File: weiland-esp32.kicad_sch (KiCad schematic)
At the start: 19 parts, among them J1 Conn_01x04_Pin, J3 Conn_01x04_Pin, J5 Conn_02x03_Odd_Even, U1 ESP32-WROOM-32E(8MB), U2 AMS1117-3.3_C347222, U3 GR6205-SOP-8, U4 MAX98357AEWL_T

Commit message: routing draft completed
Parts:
- removed J3: Conn_01x04_Pin, Connector_Wire:SolderWire-0.75sqmm_1x04_P4.8mm_D1.25mm_OD2.3mm, symbol Connector:Conn_01x04_Pin
- added J2: Conn_01x05_Pin, customlibrary:SolderWire-0.75sqmm_1x05_P4.8mm_D1.25mm_OD2.3mm, symbol Connector:Conn_01x05_Pin
- J5: footprint (none) -> Connector_PinSocket_1.27mm:PinSocket_2x03_P1.27mm_Vertical_SMD
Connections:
- net +5V_EXT is gone; now on net +5V: C3.2, J5.2 (Pin_2)
- net +5V: now also U4.A1 (SD_MODE), J2.5 (Pin_5)
- net GND: now also J2.4 (Pin_4)
- net OUTB: now also J2.3 (Pin_3)
- net OUTN: now also J2.2 (Pin_2)
- net OUTP: now also J2.1 (Pin_1)
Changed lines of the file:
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@@
 	(wire
 		(pts
-			(xy 55.88 60.96) (xy 44.45 60.96)
+			(xy 35.56 60.96) (xy 27.94 60.96)
 		)
 		(stroke
@@
 	(wire
 		(pts
-			(xy 44.45 55.88) (xy 52.07 55.88)
+			(xy 27.94 55.88) (xy 31.75 55.88)
 		)
 		(stroke
@@
 	(wire
 		(pts
-			(xy 44.45 58.42) (xy 52.07 58.42)
+			(xy 27.94 58.42) (xy 31.75 58.42)
 		)
 		(stroke
@@
 	(wire
 		(pts
+			(xy 218.44 173.99) (xy 219.71 173.99)
+		)
+		(stroke
+			(width 0)
+			(type default)
+		)
+	)
+	(wire
+		(pts
 			(xy 57.15 119.38) (xy 36.83 119.38)
 		)
@@
 	(wire
 		(pts
+			(xy 218.44 179.07) (xy 218.44 173.99)
+		)
+		(stroke
+			(width 0)
+			(type default)
+		)
+	)
+	(wire
+		(pts
 			(xy 255.27 163.83) (xy 295.91 163.83)
 		)
@@
 	(wire
 		(pts
+			(xy 27.94 66.04) (xy 30.48 66.04)
+		)
+		(stroke
+			(width 0)
+			(type default)
+		)
+	)
+	(wire
+		(pts
 			(xy 295.91 193.04) (xy 295.91 198.12)
 		)
@@
 	(wire
 		(pts
-			(xy 44.45 63.5) (xy 57.15 63.5)
+			(xy 27.94 63.5) (xy 36.83 63.5)
 		)
 		(stroke
@@
 	(wire
 		(pts
+			(xy 30.48 66.04) (xy 30.48 71.12)
+		)
+		(stroke
+			(width 0)
+			(type default)
+		)
+	)
+	(wire
+		(pts
 			(xy 124.46 30.48) (xy 124.46 39.37)
 		)
@@
 	)
 	(label "OUTB"
-		(at 54.61 60.96 0)
+		(at 34.29 60.96 0)
 		(fields_autoplaced yes)
 		(effects
@@
 	)
 	(label "OUTP"
-		(at 49.53 55.88 0)
+		(at 29.21 55.88 0)
 		(fields_autoplaced yes)
 		(effects
@@
 	)
 	(label "OUTN"
-		(at 50.8 58.42 0)
+		(at 30.48 58.42 0)
 		(fields_autoplaced yes)
 		(effects
@@
 	)
 	(symbol
-		(lib_id "Connector:Conn_01x04_Pin")
-		(at 39.37 58.42 0)
+		(lib_id "+5V")
+		(at 218.44 179.07 0)
+		(mirror y)
 		(unit 1)
 		(exclude_from_sim no)
@@
 		(on_board yes)
 		(dnp no)
-		(fields_autoplaced yes)
-		(property "Reference" "J3"
-			(at 40.005 50.8 0)
+		(property "Reference" "#PWR03"
+			(at 218.44 179.07 0)
 			(effects
 				(font
 					(size 1.27 1.27)
 				)
+				(hide yes)
 			)
 		)
-		(property "Value" "Conn_01x04_Pin"
-			(at 40.005 53.34 0)
+		(property "Value" "+5V"
+			(at 221.6912 182.0926 0)
 			(effects
 				(font
-					(size 1.27 1.27)
+					(face "Times New Roman")
+					(size 2.1717 2.1717)
 				)
+				(justify left top)
 			)
 		)
-		(property "Footprint" "Connector_Wire:SolderWire-0.75sqmm_1x04_P4.8mm_D1.25mm_OD2.3mm"
-			(at 39.37 58.42 0)
+		(property "Footprint" ""
+			(at 218.44 179.07 0)
 			(effects
 				(font
@@
 			)
 		)
-		(property "Datasheet" "~"
-			(at 39.37 58.42 0)
+		(property "Datasheet" ""
+			(at 218.44 179.07 0)
 			(effects
 				(font
@@
 			)
 		)
-		(property "Description" "Generic connector, single row, 01x04, script generated"
-			(at 39.37 58.42 0)
+		(property "Description" "Power symbol creates a global label with name '+5V'"
+			(at 218.44 179.07 0)
 			(effects
 				(font
@@
 			)
 		)
-		(pin "4"
-		)
-		(pin "2"
-		)
-		(pin "3"
-		)
 		(pin "1"
 		)
 		(instances
-			(project "esp32-online-design"
+			(project "weiland-esp32"
 				(path "/745a8d65-fa51-45f7-9665-7610e72f2a80"
-					(reference "J3")
-					(unit 1)
-				)
-			)
-			(project ""
-				(path "/a1dc64ca-b54e-4a93-b40f-f15a664195f8"
-					(reference "J6")
+					(reference "#PWR03")
 					(unit 1)
 				)
@@
 	)
 	(symbol
+		(lib_id "Connector:Conn_01x05_Pin")
+		(at 22.86 60.96 0)
+		(unit 1)
+		(exclude_from_sim no)
+		(in_bom yes)
+		(on_board yes)
+		(dnp no)
+		(fields_autoplaced yes)
+		(property "Reference" "J2"
+			(at 23.495 50.8 0)
+			(effects
+				(font
+					(size 1.27 1.27)
+				)
+			)
+		)
+		(property "Value" "Conn_01x05_Pin"
+			(at 23.495 53.34 0)
+			(effects
+				(font
+					(size 1.27 1.27)
+				)
+			)
+		)
+		(property "Footprint" "customlibrary:SolderWire-0.75sqmm_1x05_P4.8mm_D1.25mm_OD2.3mm"
+			(at 22.86 60.96 0)
+			(effects
+				(font
+					(size 1.27 1.27)
+				)
+				(hide yes)
+			)
+		)
+		(property "Datasheet" "~"
+			(at 22.86 60.96 0)
+			(effects
+				(font
+					(size 1.27 1.27)
+				)
+				(hide yes)
+			)
+		)
+		(property "Description" "Generic connector, single row, 01x05, script generated"
+			(at 22.86 60.96 0)
+			(effects
+				(font
+					(size 1.27 1.27)
+				)
+				(hide yes)
+			)
+		)
+		(pin "2"
+		)
+		(pin "1"
+		)
+		(pin "4"
+		)
+		(pin "5"
+		)
+		(pin "3"
+		)
+		(instances
+			(project ""
+				(path "/745a8d65-fa51-45f7-9665-7610e72f2a80"
+					(reference "J2")
+					(unit 1)
+				)
+			)
+		)
+	)
+	(symbol
 		(lib_id "CL21A226MAYNNNE")
 		(at 13.97 105.41 0)
@@
 			)
 		)
-		(property "Footprint" ""
+		(property "Footprint" "Connector_PinSocket_1.27mm:PinSocket_2x03_P1.27mm_Vertical_SMD"
 			(at 104.14 30.48 0)
 			(effects
@@
 	)
 	(symbol
-		(lib_id "+5V_EXT")
-		(at 129.54 25.4 0)
-		(mirror x)
+		(lib_id "+5V")
+		(at 30.48 71.12 0)
+		(mirror y)
 		(unit 1)
 		(exclude_from_sim no)
@@
 		(on_board yes)
 		(dnp no)
-		(property "Reference" "#PWR0104"
-			(at 129.54 25.4 0)
+		(property "Reference" "#PWR02"
+			(at 30.48 71.12 0)
 			(effects
 				(font
@@
 			)
 		)
-		(property "Value" "+5V_EXT"
-			(at 121.4628 21.6154 0)
+		(property "Value" "+5V"
+			(at 33.7312 74.1426 0)
 			(effects
 				(font
@@
 		)
 		(property "Footprint" ""
-			(at 129.54 25.4 0)
+			(at 30.48 71.12 0)
 			(effects
 				(font
@@
 		)
 		(property "Datasheet" ""
-			(at 129.54 25.4 0)
+			(at 30.48 71.12 0)
 			(effects
 				(font
@@
 			)
 		)
-		(property "Description" "Power symbol creates a global label with name '+5V_EXT'"
-			(at 129.54 25.4 0)
+		(property "Description" "Power symbol creates a global label with name '+5V'"
+			(at 30.48 71.12 0)
 			(effects
 				(font
@@
 		)
 		(instances
-			(project "esp32-online-design"
+			(project "weiland-esp32"
 				(path "/745a8d65-fa51-45f7-9665-7610e72f2a80"
-					(reference "#PWR0104")
+					(reference "#PWR02")
 					(unit 1)
 				)
@@
 	(symbol
 		(lib_id "GND")
-		(at 57.15 63.5 90)
+		(at 36.83 63.5 90)
 		(unit 1)
 		(exclude_from_sim no)
@@
 		(dnp no)
 		(property "Reference" "#PWR0101"
-			(at 57.15 63.5 0)
+			(at 36.83 63.5 0)
 			(effects
 				(font
@@
 		)
 		(property "Value" "GND"
-			(at 63.754 66.802 0)
+			(at 43.434 66.802 0)
 			(effects
 				(font
@@
 		)
 		(property "Footprint" ""
-			(at 57.15 63.5 0)
+			(at 36.83 63.5 0)
 			(effects
 				(font
@@
 		)
 		(property "Datasheet" ""
-			(at 57.15 63.5 0)
+			(at 36.83 63.5 0)
 			(effects
 				(font
@@
 		)
 		(property "Description" "Power symbol creates a global label with name 'GND'"
-			(at 57.15 63.5 0)
+			(at 36.83 63.5 0)
 			(effects
 				(font
@@
 				)
 			)
+		)
+	)
+	(symbol
+		(lib_id "+5V")
+		(at 129.54 25.4 0)
+		(mirror x)
+		(unit 1)
+		(exclude_from_sim no)
+		(in_bom yes)
+		(on_board yes)
+		(dnp no)
+		(property "Reference" "#PWR01"
+			(at 129.54 25.4 0)
+			(effects
+				(font
+					(size 1.27 1.27)
+				)
+				(hide yes)
+			)
+		)
+		(property "Value" "+5V"
+			(at 126.2888 22.3774 0)
+			(effects
+				(font
+					(face "Times New Roman")
+					(size 2.1717 2.1717)
+				)
+				(justify left top)
+			)
+		)
+		(property "Footprint" ""
+			(at 129.54 25.4 0)
+			(effects
+				(font
+					(size 1.27 1.27)
+				)
+				(hide yes)
+			)
+		)
+		(property "Datasheet" ""
+			(at 129.54 25.4 0)
+			(effects
+				(font
+					(size 1.27 1.27)
+				)
+				(hide yes)
+			)
+		)
+		(property "Description" "Power symbol creates a global label with name '+5V'"
+			(at 129.54 25.4 0)
+			(effects
+				(font
+					(size 1.27 1.27)
+				)
+				(hide yes)
+			)
+		)
+		(pin "1"
+		)
+		(instances
+			(project "weiland-esp32"
+				(path "/745a8d65-fa51-45f7-9665-7610e72f2a80"
+					(reference "#PWR01")
+					(unit 1)
+				)
+			)

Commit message: last commit before 4 motor branch
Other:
- note added: "ESP32 Custom Board"
- note removed: "Custom ESP32"
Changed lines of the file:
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@@
 		)
 	)
-	(text "Custom ESP32\n"
+	(text "ESP32 Custom Board"
 		(exclude_from_sim no)
 		(at 165.1 8.4836 0)

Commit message: jst connectors
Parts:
- removed J1: Conn_01x04_Pin, Connector_Wire:SolderWire-0.75sqmm_1x04_P4.8mm_D1.25mm_OD2.3mm, symbol Connector:Conn_01x04_Pin
- removed J2: Conn_01x05_Pin, customlibrary:SolderWire-0.75sqmm_1x05_P4.8mm_D1.25mm_OD2.3mm, symbol Connector:Conn_01x05_Pin
- removed J5: Conn_02x03_Odd_Even, Connector_PinSocket_1.27mm:PinSocket_2x03_P1.27mm_Vertical_SMD, symbol Connector_Generic:Conn_02x03_Odd_Even
- added J1, J3, J4, J6, J7: S02B-PASK-2, footprints:CONN2_S02B-PASK-2_JST, symbol jst2pin:S02B-PASK-2
- added J2: 20021221-00006T4LF, dc3-6p:dc3-6p, symbol dc3-6p:20021221-00006T4LF
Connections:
- net +5V: now also J2.2, J6.2
- net EN: now also J2.1
- net GND: now also J2.4, J3.1, J4.1, J6.1
- net IO0: now also J2.6
- net OUTA: now also J4.2
- net OUTB: now also J3.2
- net OUTN: now also J1.2, J7.2
- net OUTP: now also J1.1, J7.1
- net RXD0: now also J2.5
- net TXD0: now also J2.3
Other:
- moved on the sheet: C1, C2, C3, U1

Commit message: good schematic before unshrouded header
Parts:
- removed J3, J4: S02B-PASK-2, footprints:CONN2_S02B-PASK-2_JST, symbol jst2pin:S02B-PASK-2
- removed U3: GR6205-SOP-8, motor_driver:SOP127P780X200-8N, symbol GR6205-SOP-8:GR6205-SOP-8
- added P1, P2: S04B-PASK-2_LF__SN_, S04B-PASK-2_LF__SN_:JST_S04B-PASK-2, symbol S04B-PASK-2:S04B-PASK-2_LF__SN_
- added U5: ULN2003F12FN-7, ULN2003:U-DFN3030-10_DIO, symbol ULN2003:ULN2003F12FN-7
- C1: footprint 22uF capacitor:CAPC1608X90N -> 100ohm-resistor:RESC1005X40N
- C4, C5: value 10uF -> 22uF; footprint 10 uF capacitor:CAPC1608X90N -> 100ohm-resistor:RESC1005X40N
- C6: footprint 10 uF capacitor:CAPC1608X90N -> 100ohm-resistor:RESC1005X40N
- C7, C8: footprint 220pF capacitor:CAPC1005X55N -> 100ohm-resistor:RESC1005X40N
- R1: value 5.1kΩ -> 100Ω; footprint 5-1-ohm-resistor:RES_ERJ2RKF5101X -> 100ohm-resistor:RESC1005X40N
- U4: footprint MAX98357AEWL_T:BGA9N40P3X3_134X143X69N -> MAX98357AETE_T:QFN50P300X300X80-17N
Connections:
- net +3V3: now also U4.A1 (SD_MODE)
- net +5V: now also P1.1, P1.3, P2.1, P2.3; no longer U4.A1 (SD_MODE)
- net GND: now also U5.11 (EPAD), U5.5 (GND)
- net OUTA: now also P2.2, U5.10 (OUT1)
- net OUTB: now also P2.4, U5.9 (OUT2)
- net IO14: now reaches U1.13 (IO14)
- net IO14: now also U4.C3 (LRCLK)
- net IO15: now reaches U1.23 (IO15)
- net IO15: now also U4.C1 (BCLK)
- net IO16: now reaches U1.27 (IO16)
- net IO16: now also U5.4 (IN4)
- net IO17: now reaches U1.28 (IO17)
- net IO17: now also U5.3 (IN3)
- net IO18: now reaches U1.30 (IO18)
- net IO18: now also U5.2 (IN2)
- net IO19: now reaches U1.31 (IO19)
- net IO19: now also U5.1 (IN1)
- net IO22: now reaches U1.36 (IO22)
- net IO22: now also U4.B1 (DIN)
- net IO25: no longer names the net of U1.10 (IO25)
- net IO25: no longer U4.B1 (DIN)
- net IO26: no longer names the net of U1.11 (IO26)
- net IO26: no longer U4.C3 (LRCLK)
- net IO27: no longer names the net of U1.12 (IO27)
- net IO27: no longer U4.C1 (BCLK)
- net IO32: no longer names the net of U1.8 (IO32)
- net IO33: no longer names the net of U1.9 (IO33)
- new net OUTC: P1.4, U5.8 (OUT3)
- new net OUTD: P1.2, U5.7 (OUT4)
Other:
- note added: "Audio Amp"
- note added: "Glasses Embedded Module (GEM)"
- note added: "Motor Controller"
- note removed: "ESP32 Custom Board"
- note removed: "Motors and Audio"
- moved on the sheet: C1, C2, C3, C4, C5, C6, C7, C8, FB1, FB2, J1, J2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

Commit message: test point schematic, before adding to layout
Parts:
- removed J2: 20021221-00006T4LF, dc3-6p:dc3-6p, symbol dc3-6p:20021221-00006T4LF
- removed U4: MAX98357AEWL_T, MAX98357AETE_T:QFN50P300X300X80-17N, symbol MAX98357AEWL_T:MAX98357AEWL_T
- added C9: 0.1uF, Capacitor_SMD:C_0402_1005Metric, symbol Device:C
- added R2: 10k, Resistor_SMD:R_0402_1005Metric, symbol Device:R_US
- added TP12, TP13, TP14, TP2, TP4, TP5, TP6, TP7: TestPoint, symbol Connector:TestPoint
- added U3: MAX98357AETE_T, MAX98357AETE_T:QFN50P300X300X80-17N, symbol MAX98357AETE_T:MAX98357AETE_T
- added U6: DZ127S-22-06-55, unshroudedheader:HDR-SMD_6P-P1.27-V-M-R2-C3-S1.27-LS5.5-1, symbol unshroudedheader:DZ127S-22-06-55
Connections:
- net +5V: now also U3.7 (VDD), U3.8 (VDD__1), U6.2
- net EN: now also C9.1, R2.2, U6.1
- net GND: now also C9.2, U3.11 (GND__1), U3.15 (GND__2), U3.17 (EP), U3.2 (GAIN_SLOT), U3.3 (GND), U6.4
- net IO0: now also U6.6
- net IO14: now also TP14.1, U3.14 (LRCLK)
- net IO15: now also TP12.1, U3.16 (BCLK)
- net IO16: now also TP7.1
- net IO17: now also TP6.1
- net IO18: now also TP5.1
- net IO19: now also TP4.1
- net IO22: now also TP13.1, U3.1 (DIN)
- net OUTC: now also P1.2; no longer P1.4
- net OUTD: now also P1.4; no longer P1.2
- net OUTN: now also J1.1; no longer J1.2
- net OUTP: now also J1.2; no longer J1.1
- net RXD0: now also U6.5
- net TXD0: now also U6.3
- net at FB1.1: now also U3.9 (OUTP)
- net at FB2.1: now also U3.10 (OUTN)
- net +3V3 renamed +3.3V
- net +3.3V: now also R2.1, TP2.1, U3.4 (SD_MODE)
- no-connect marks 7 -> 24
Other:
- note added: "TEST POINTS"
- moved on the sheet: C1, C2, C4, C5, C6, C7, C8, FB1, FB2, J6, LED1, P1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

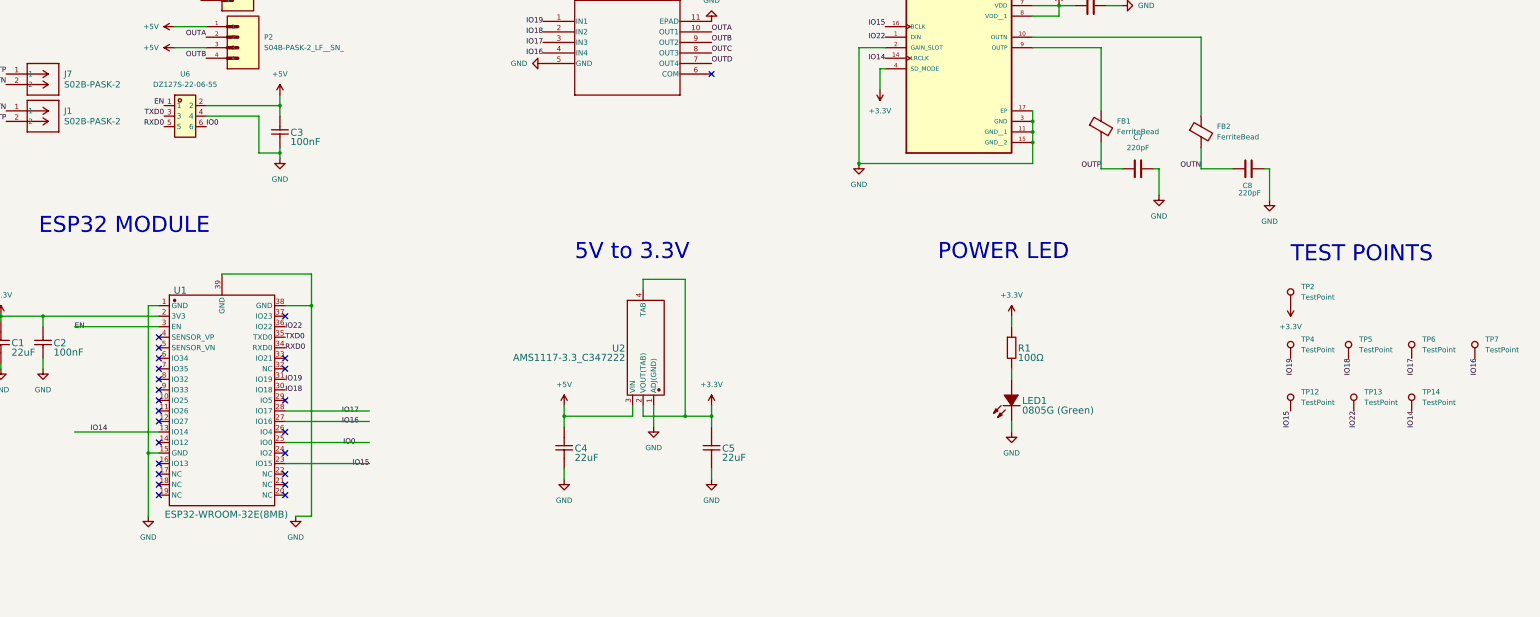
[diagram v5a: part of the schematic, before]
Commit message: 52x39 board w/ holes
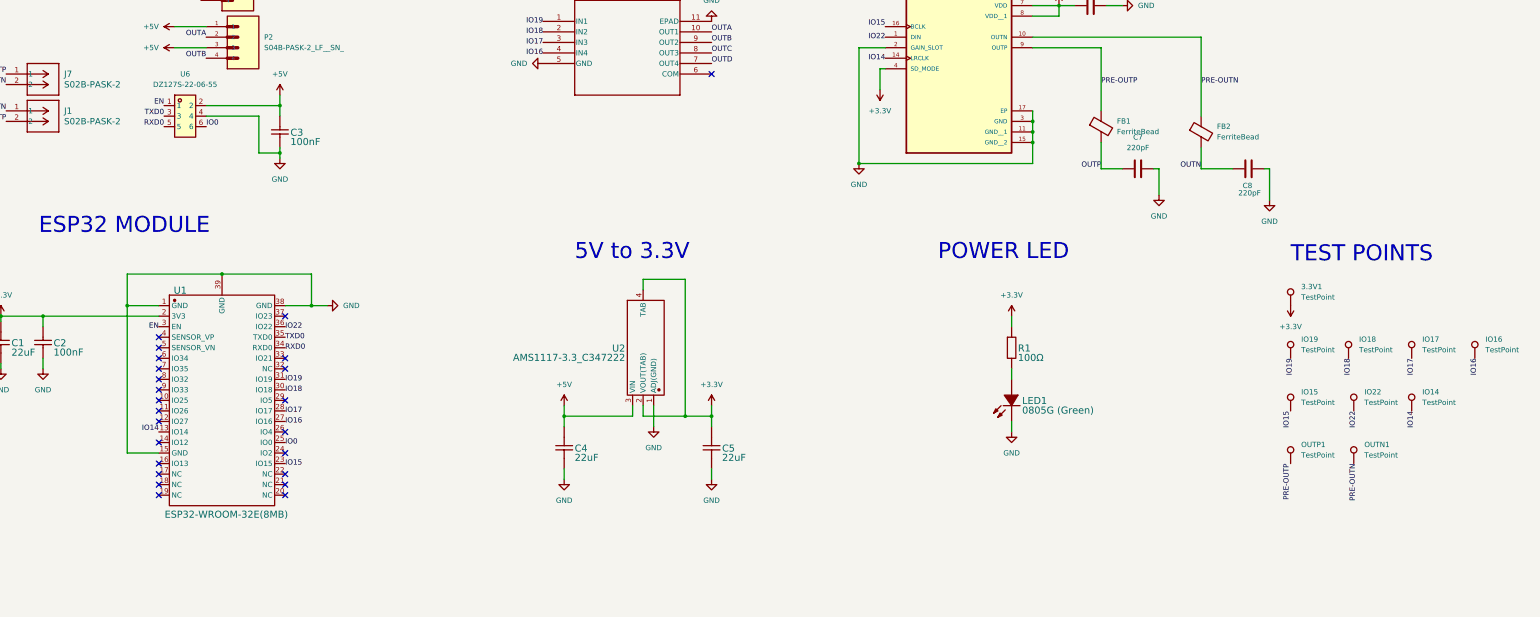
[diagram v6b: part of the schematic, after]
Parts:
- removed TP12, TP13, TP14, TP2, TP4, TP5, TP6, TP7: TestPoint, symbol Connector:TestPoint
- added 3.3V1, IO14, IO15, IO16, IO17, IO18, IO19, IO22, OUTN1, OUTP1: TestPoint, TestPoint:TestPoint_Pad_D1.0mm, symbol Connector:TestPoint
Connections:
- net +3.3V: now also 3.3V1.1
- net IO14: now also IO14.1
- net IO15: now also IO15.1
- net IO16: now also IO16.1
- net IO17: now also IO17.1
- net IO18: now also IO18.1
- net IO19: now also IO19.1
- net IO22: now also IO22.1
- net PRE-OUTN: now reaches FB2.1, U3.10 (OUTN)
- net PRE-OUTN: now also OUTN1.1
- net PRE-OUTP: now reaches FB1.1, U3.9 (OUTP)
- net PRE-OUTP: now also OUTP1.1

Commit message: before deleting all traces
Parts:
- added H1, H2: MountingHole, MountingHole:MountingHole_3.2mm_M3, symbol Mechanical:MountingHole
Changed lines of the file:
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@@
 	)
 	(symbol
+		(lib_id "Mechanical:MountingHole")
+		(at 372.11 175.26 0)
+		(unit 1)
+		(exclude_from_sim yes)
+		(in_bom no)
+		(on_board yes)
+		(dnp no)
+		(fields_autoplaced yes)
+		(property "Reference" "H1"
+			(at 374.65 173.9899 0)
+			(effects
+				(font
+					(size 1.27 1.27)
+				)
+				(justify left)
+			)
+		)
+		(property "Value" "MountingHole"
+			(at 374.65 176.5299 0)
+			(effects
+				(font
+					(size 1.27 1.27)
+				)
+				(justify left)
+			)
+		)
+		(property "Footprint" "MountingHole:MountingHole_3.2mm_M3"
+			(at 372.11 175.26 0)
+			(effects
+				(font
+					(size 1.27 1.27)
+				)
+				(hide yes)
+			)
+		)
+		(property "Datasheet" "~"
+			(at 372.11 175.26 0)
+			(effects
+				(font
+					(size 1.27 1.27)
+				)
+				(hide yes)
+			)
+		)
+		(property "Description" "Mounting Hole without connection"
+			(at 372.11 175.26 0)
+			(effects
+				(font
+					(size 1.27 1.27)
+				)
+				(hide yes)
+			)
+		)
+		(instances
+			(project ""
+				(path "/745a8d65-fa51-45f7-9665-7610e72f2a80"
+					(reference "H1")
+					(unit 1)
+				)
+			)
+		)
+	)
+	(symbol
 		(lib_id "jst2pin:S02B-PASK-2")
 		(at 27.94 45.72 0)
@@
 					(unit 1)
 				)
+			)
+		)
+	)
+	(symbol
+		(lib_id "Mechanical:MountingHole")
+		(at 372.11 181.61 0)
+		(unit 1)
+		(exclude_from_sim yes)
+		(in_bom no)
+		(on_board yes)
+		(dnp no)
+		(fields_autoplaced yes)
+		(property "Reference" "H2"
+			(at 374.65 180.3399 0)
+			(effects
+				(font
+					(size 1.27 1.27)
+				)
+				(justify left)
+			)
+		)
+		(property "Value" "MountingHole"
+			(at 374.65 182.8799 0)
+			(effects
+				(font
+					(size 1.27 1.27)
+				)
+				(justify left)
+			)
+		)
+		(property "Footprint" "MountingHole:MountingHole_3.2mm_M3"
+			(at 372.11 181.61 0)
+			(effects
+				(font
+					(size 1.27 1.27)
+				)
+				(hide yes)
+			)
+		)
+		(property "Datasheet" "~"
+			(at 372.11 181.61 0)
+			(effects
+				(font
+					(size 1.27 1.27)
+				)
+				(hide yes)
+			)
+		)
+		(property "Description" "Mounting Hole without connection"
+			(at 372.11 181.61 0)
+			(effects
+				(font
+					(size 1.27 1.27)
+				)
+				(hide yes)
+			)
+		)
+		(instances
+			(project "weiland-esp32"
+				(path "/745a8d65-fa51-45f7-9665-7610e72f2a80"
+					(reference "H2")
+					(unit 1)
+				)
